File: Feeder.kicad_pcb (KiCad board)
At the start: 4 copper layers, 91 x 85 mm, 89 parts, among them J101 Conn_02x03_Odd_Even, J102 Conn_01x03_Pin, J103 Conn_01x02_Pin, U101 XBLW 24C02S(XBLW), U201 CMP6793RE, U301 CMP6793RE, U601 TPS562202, U701 TPS562202

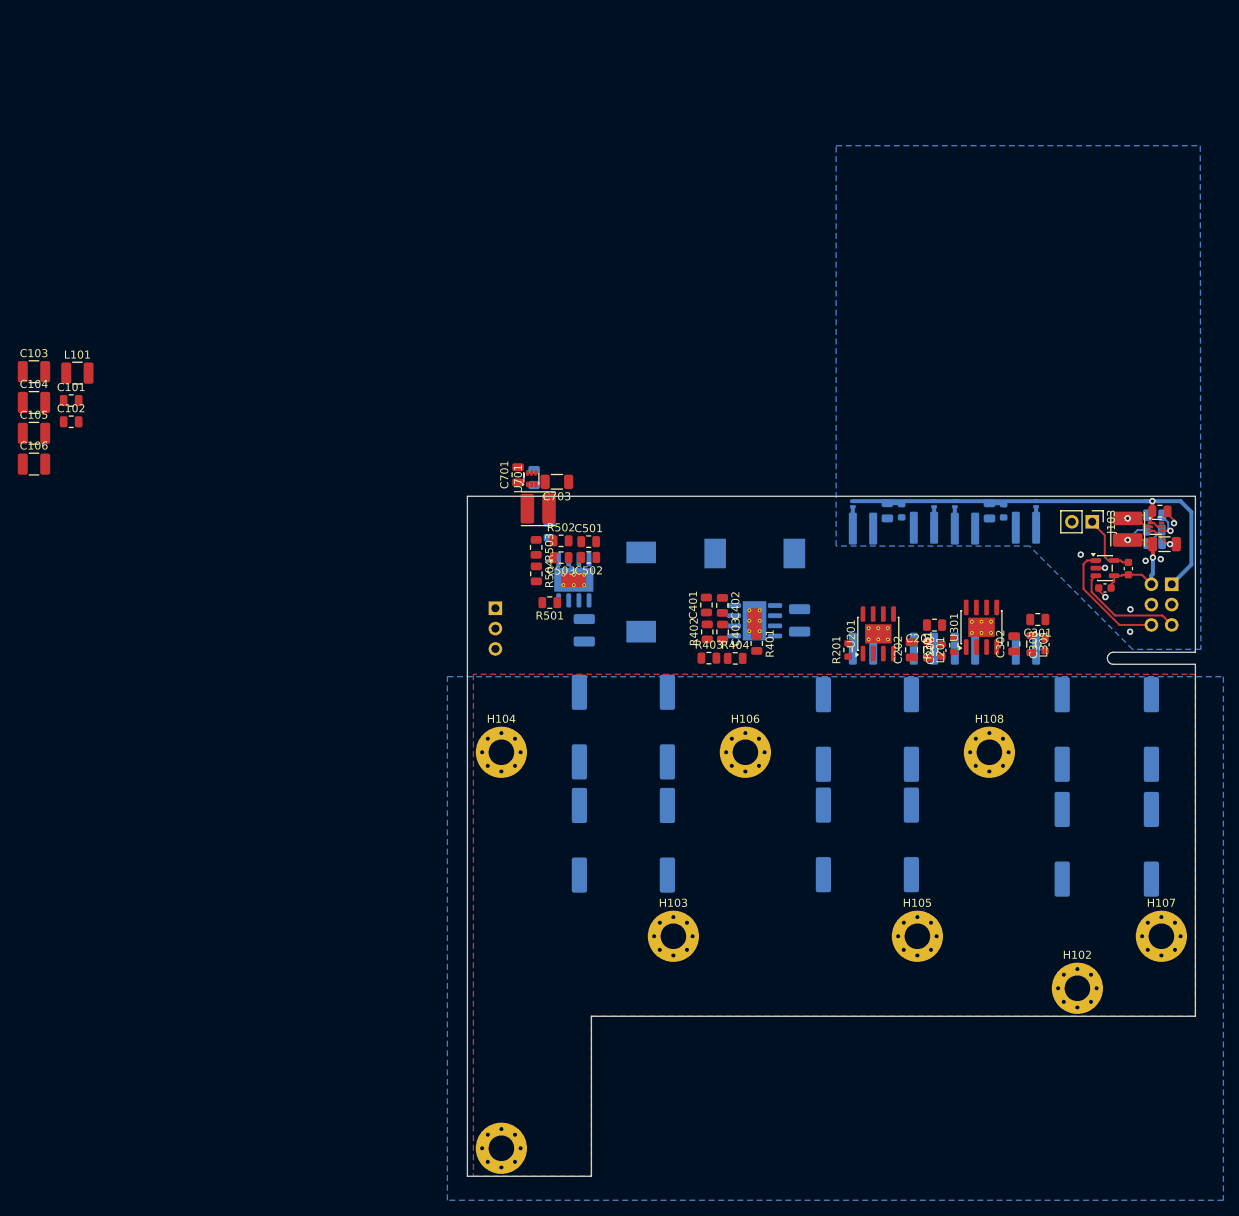
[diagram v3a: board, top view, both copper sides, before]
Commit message: feeder is routed
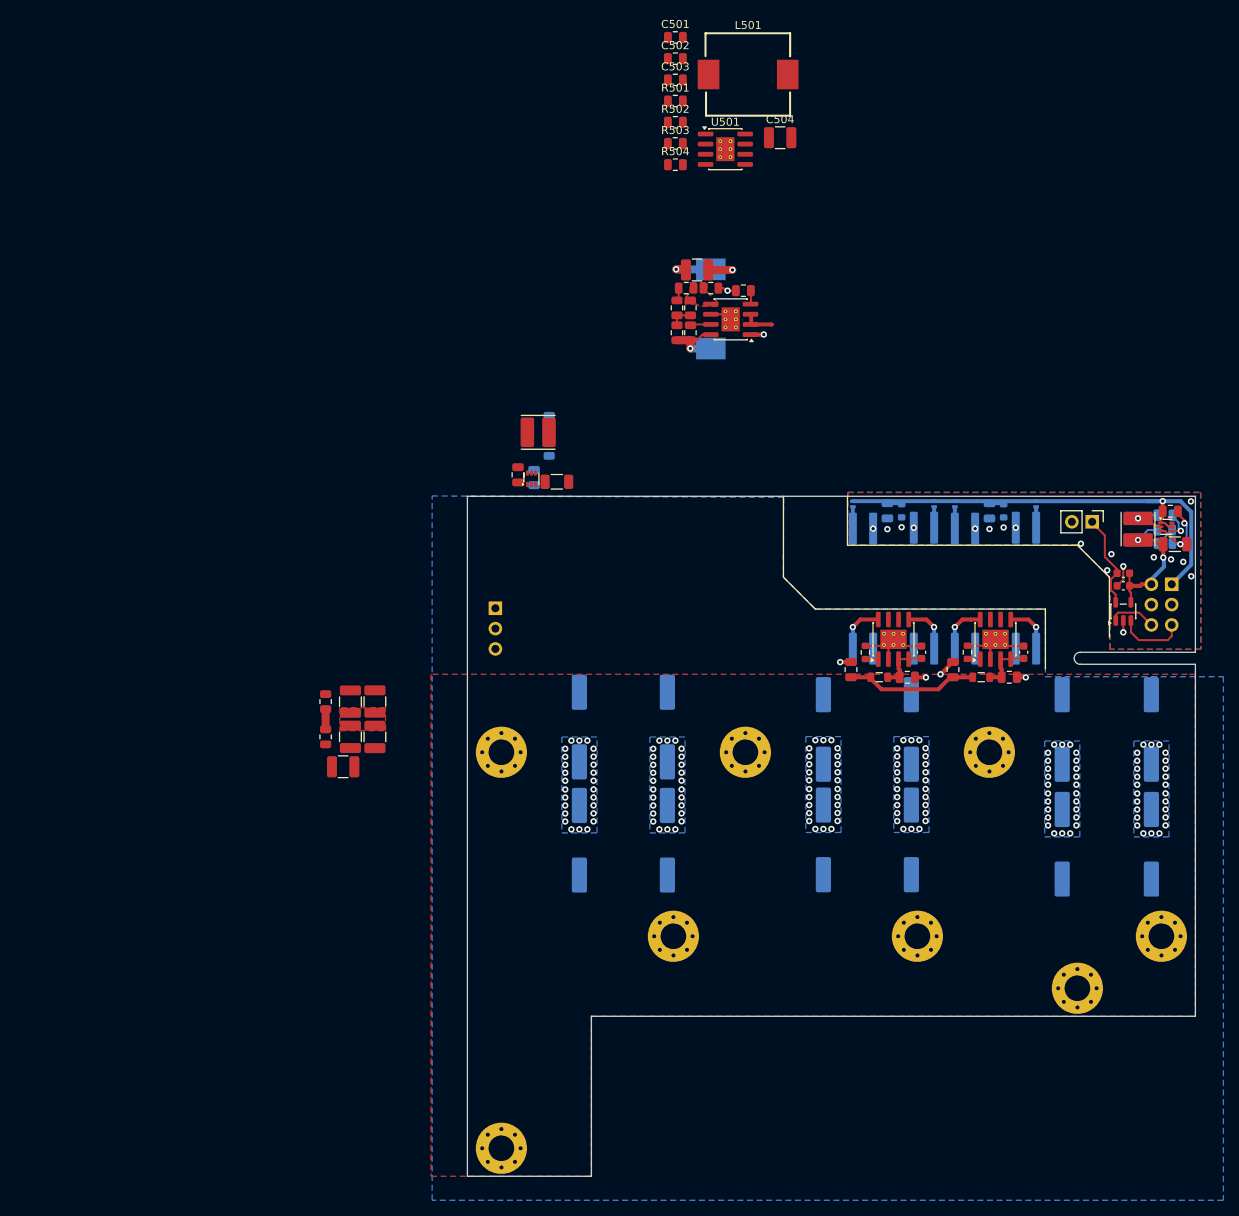
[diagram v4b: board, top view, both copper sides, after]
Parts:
- C404, C504, L501: moved to F.Cu
- U401, U501: footprint Package_SO:Texas_R-PDSO-G8_EP2.95x4.9mm_Mask2.4x3.1mm_ThermalVias -> Package_SO:SOIC-8-1EP_3.9x4.9mm_P1.27mm_EP2.29x3mm_ThermalVias; moved to F.Cu
- moved C504 66.3 mm to (43.6, -139.8), turned to 0 degrees
- moved L501 66.1 mm to (39.6, -147.7), turned to 0 degrees
- moved R501 64.6 mm to (30.5, -144.4), turned to 0 degrees
- moved C501 63.9 mm to (30.5, -152.3)
- moved C502 63.3 mm to (30.5, -149.7), turned to 0 degrees
- moved C503 61.4 mm to (30.5, -147.1), turned to 0 degrees
- moved C103 60.4 mm to (-10.1, -64.9), turned to 90 degrees
- moved L101 59.4 mm to (-11.0, -61.2), turned to 180 degrees
- moved U501 57.1 mm to (36.7, -138.4), turned to 0 degrees
- moved C105 57.1 mm to (-7.06, -64.9), turned to 90 degrees
- moved C104 54.4 mm to (-10.1, -69.3), turned to 90 degrees
- moved R502 54.2 mm to (30.5, -141.8)
- moved R504 54.0 mm to (30.5, -136.4), turned to 0 degrees
- moved R503 53.4 mm to (30.5, -139.1), turned to 0 degrees
- moved C101 52.7 mm to (-13.2, -64.9), turned to 90 degrees
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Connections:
- U401 pad 9: (no net) -> PGND
- U501 pad 9: (no net) -> PGND
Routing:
- net PGND: track 0.00 -> 30.6 mm, vias 0 -> 7
- net /buck/VOUT: track 0.00 -> 23.7 mm, vias 0 -> 1
- net Net-(U401-SW): track 0.00 -> 9.41 mm, vias 0 -> 1
- net Net-(J101-Pin_6): track 15.2 -> 5.90 mm
- net Net-(U201-EN): track 0.00 -> 6.74 mm
- net Net-(U301-EN): track 0.00 -> 6.74 mm
- net Net-(U201-VD2): track 0.00 -> 6.28 mm, vias 0 -> 1
- net Net-(U301-VD2): track 0.00 -> 6.27 mm, vias 0 -> 1
- net Net-(U301-VD1): track 0.00 -> 6.27 mm, vias 0 -> 1
- net Net-(U201-VD1): track 0.00 -> 6.26 mm, vias 0 -> 1
- net Net-(J101-Pin_5): track 14.0 -> 8.59 mm
- net DGND: track 9.14 -> 13.8 mm, vias 9 -> 20
- net /VIN_{FILT}: track 0.00 -> 3.86 mm
- net Net-(J103-Pin_1): track 8.27 -> 11.9 mm
- net Net-(C402-Pad2): track 0.00 -> 2.91 mm
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- added copper zone on B.Cu, net /VHigh
- added copper zone on F.Cu, net DGND
- added copper zone on F.Cu, net Net-(C103-Pad2)
- added copper zone on F.Cu, net Net-(U401-FB)
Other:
- outline, holes or cut-outs redrawn

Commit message: buck repeat layout done
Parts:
- L501: moved to B.Cu
- moved C501 42.1 mm to (23.6, -110.8), turned to -90 degrees
- moved L501 36.5 mm to (26.1, -113.7), turned to 90 degrees
- moved C502 36.5 mm to (23.6, -113.9), turned to -90 degrees
- moved C503 34.3 mm to (21.9, -113.9), turned to 90 degrees
- moved R502 32.1 mm to (21.9, -110.8), turned to 90 degrees
- moved C404 31.2 mm to (31.4, -92.1)
- moved C401 31.2 mm to (30.6, -84.3)
- moved C402 31.2 mm to (30.6, -87.4)
- moved C403 31.2 mm to (28.9, -87.4)
- moved L401 31.2 mm to (33.1, -87.2)
- moved R401 31.2 mm to (37.2, -89.5)
- moved R402 31.2 mm to (28.9, -84.3)
- moved R403 31.2 mm to (30.1, -89.8)
- moved R404 31.2 mm to (33.1, -89.8)
- moved U401 31.2 mm to (35.6, -85.9)
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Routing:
- net Net-(U501-SW): track 0.00 -> 9.41 mm, vias 0 -> 1
- net PGND: track 30.6 -> 39.5 mm, vias 7 -> 10
- net /buck1/VOUT: track 0.00 -> 7.16 mm, vias 0 -> 1
- net /VIN_{FILT}: track 3.86 -> 7.71 mm
- net Net-(C502-Pad2): track 0.00 -> 2.91 mm
- net Net-(U501-BST): track 0.00 -> 2.20 mm
- net Net-(U501-RT): track 0.00 -> 1.69 mm
- added copper zone on F.Cu, net Net-(U501-FB)

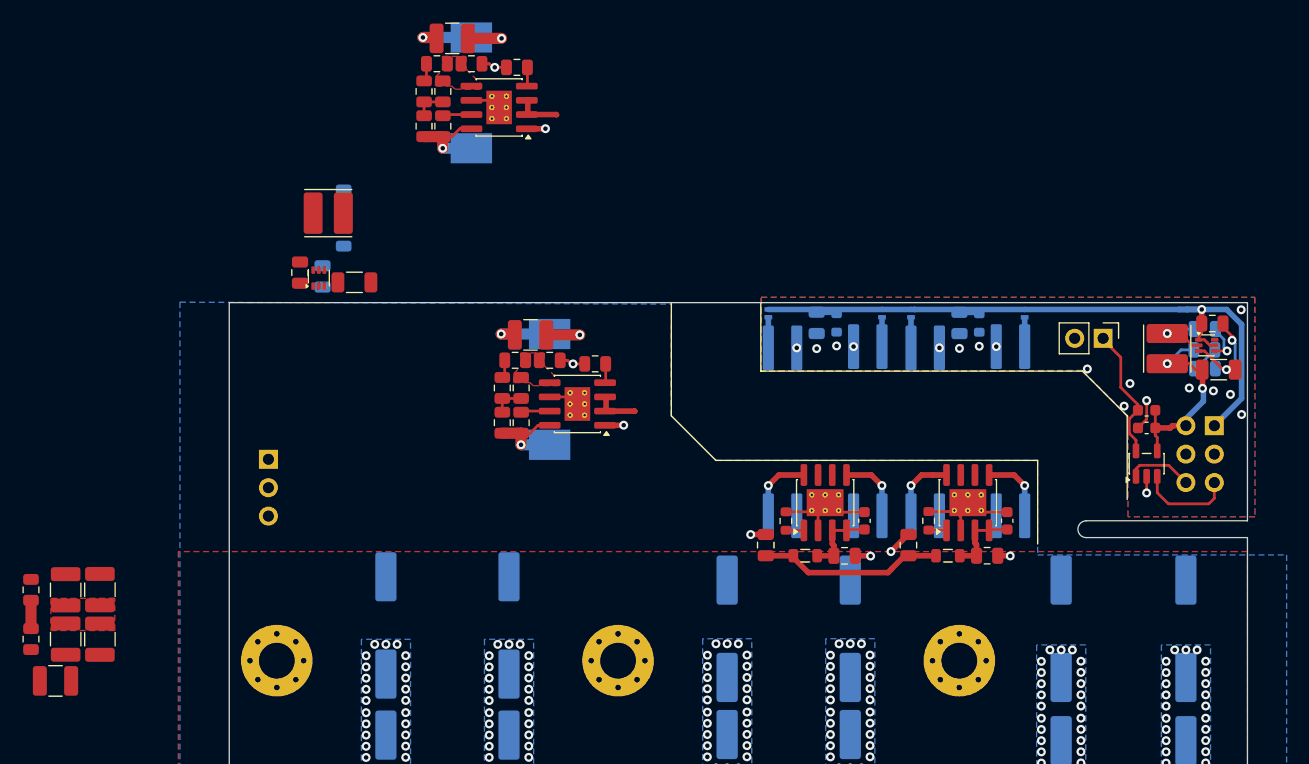
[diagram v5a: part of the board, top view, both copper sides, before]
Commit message: routing is done but violations are still present
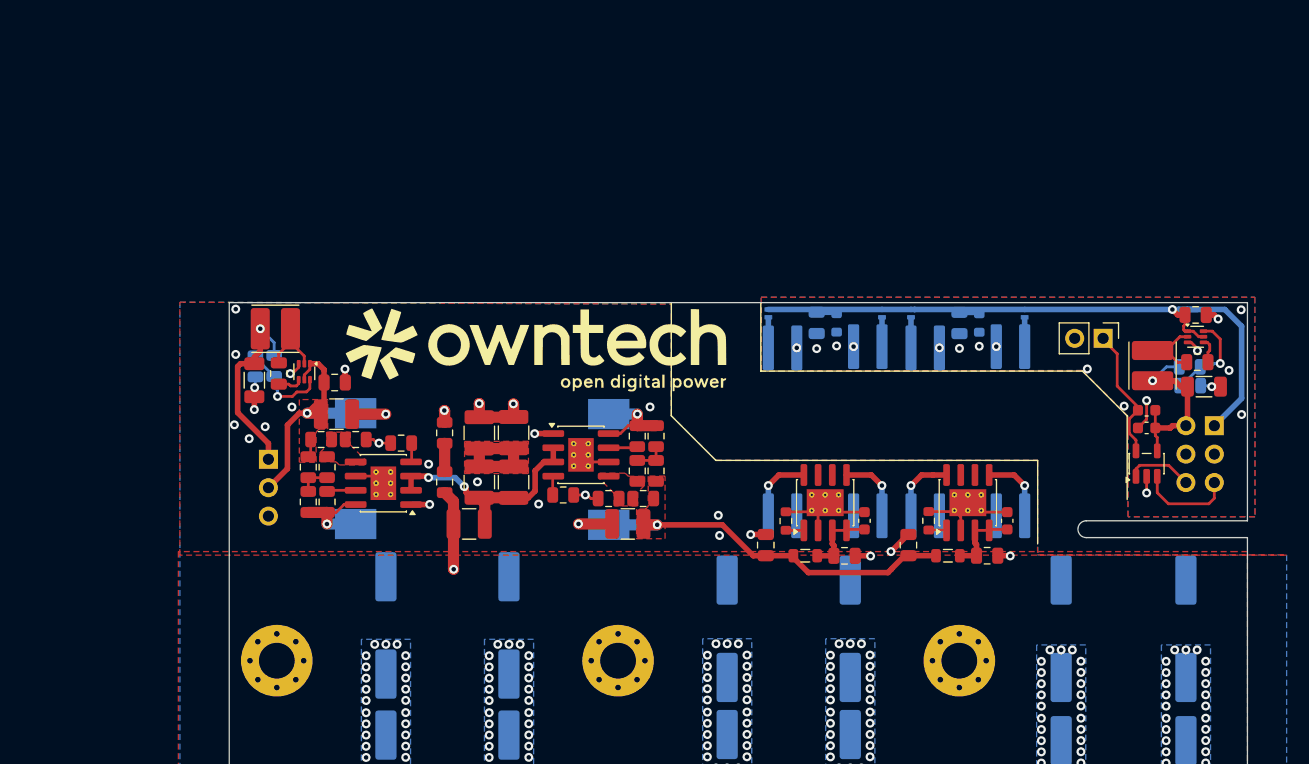
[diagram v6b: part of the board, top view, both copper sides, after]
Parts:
- added G***: LOGO, Footprints:owntech34mmneg, F.Cu at (31.9, -90.8)
- C602, C702: moved to F.Cu
- moved C101 39.5 mm to (23.8, -79.0)
- moved C102 39.5 mm to (23.8, -83.4)
- moved C103 39.5 mm to (26.9, -79.0)
- moved C104 39.5 mm to (26.9, -83.4)
- moved C105 39.5 mm to (29.9, -79.0)
- moved C106 39.5 mm to (29.9, -83.4)
- moved L101 39.5 mm to (25.9, -75.2), turned to 0 degrees
- moved C504 35.1 mm to (14.1, -85.0)
- moved R501 35.1 mm to (19.9, -82.4)
- moved C501 35.1 mm to (13.2, -77.2)
- moved C502 35.1 mm to (13.2, -80.3)
- moved C503 35.1 mm to (11.6, -80.3)
- moved L501 35.1 mm to (15.8, -80.2)
- moved R502 35.1 mm to (11.6, -77.2)
- moved R503 35.1 mm to (12.7, -82.8)
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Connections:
- J102 pad 1: /buck1/VOUT -> /dc-dc_12-6/VOUT
- J102 pad 2: /dc-dc_12-6/VOUT -> /buck1/VOUT
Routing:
- net /dc-dc_12-6/VOUT: track 0.00 -> 17.3 mm, vias 0 -> 1
- net /buck1/VOUT: track 7.16 -> 23.2 mm
- net /VIN_{FILT}: track 7.71 -> 21.2 mm, vias 0 -> 2
- net PGND: track 39.5 -> 51.8 mm, vias 10 -> 29
- net /buck/VOUT: track 23.7 -> 33.1 mm
- net Net-(C103-Pad2): track 0.00 -> 9.36 mm
- net Net-(U701-VFB): track 0.00 -> 8.42 mm, vias 0 -> 1
- net /VHigh: track 0.00 -> 7.19 mm, vias 156 -> 157
- net Net-(U701-SW): track 0.00 -> 6.90 mm
- net Net-(U601-VFB): track 2.53 -> 8.42 mm, vias 0 -> 1
- net DGND: track 13.8 -> 9.30 mm, vias 20 -> 18
- net Net-(U701-VBST): track 0.00 -> 2.27 mm
- net +5V_DGND: track 18.4 -> 16.4 mm, vias 2 -> 1
- net Net-(U601-VBST): track 3.49 -> 2.27 mm, vias 1 -> 0
- net Net-(U601-SW): track 5.84 -> 6.90 mm, vias 1 -> 0
- added copper zone on F.Cu, net /buck/VOUT
- added copper zone on F.Cu, net /buck1/VOUT
- added copper zone on F.Cu, net PGND

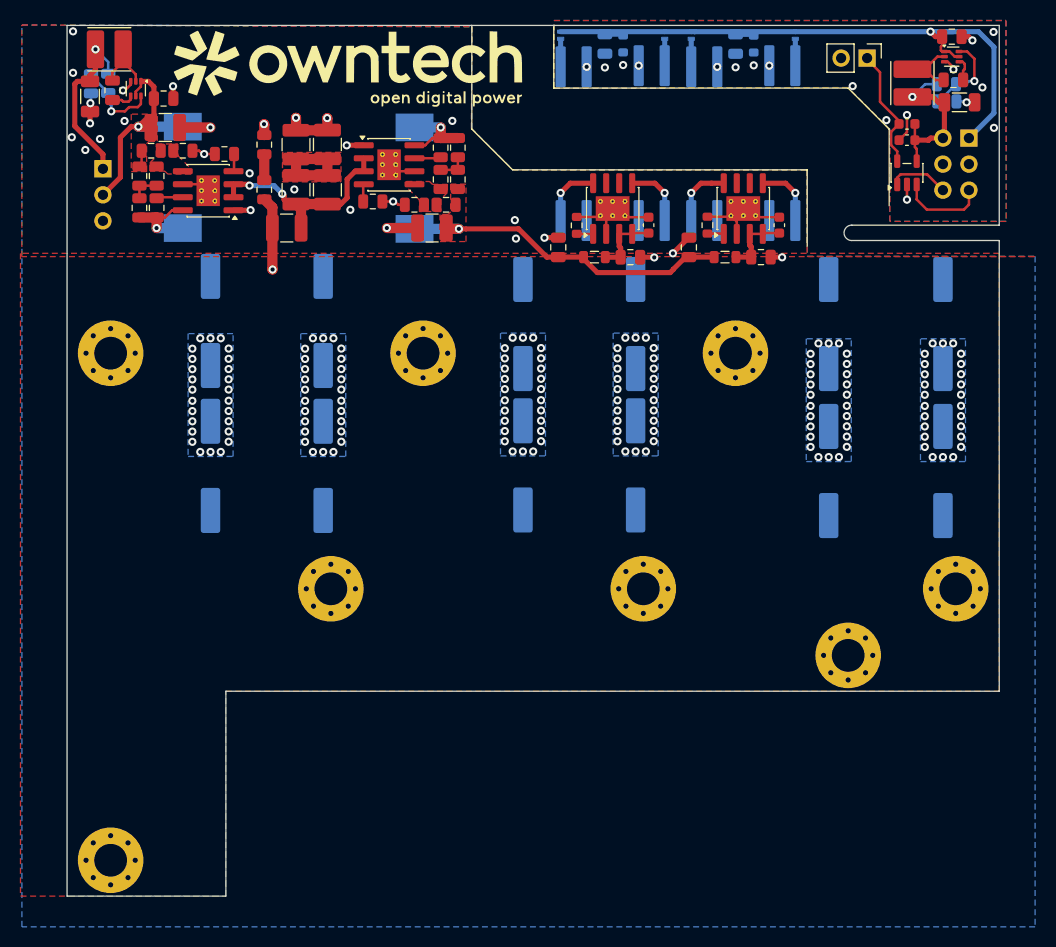
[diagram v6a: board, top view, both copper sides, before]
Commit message: no erc errors
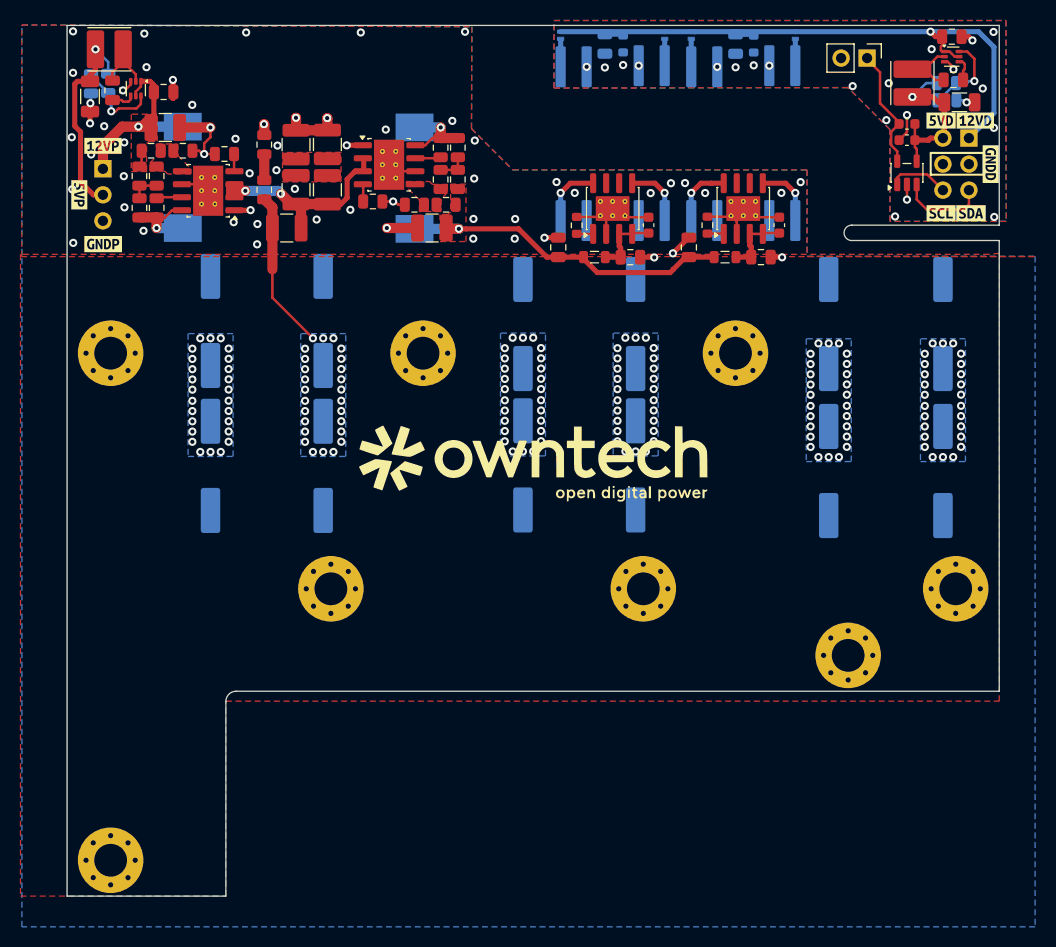
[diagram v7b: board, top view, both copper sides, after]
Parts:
- added kibuzzard-6A746332: G***, kibuzzard-6A746332, F.Cu at (5.69, -78.5)
- added kibuzzard-6A746332: G***, kibuzzard-6A746332, B.Cu at (5.69, -78.5)
- added kibuzzard-6A746339: G***, kibuzzard-6A746339, F.Cu at (8.02, -73.7)
- added kibuzzard-6A746339: G***, kibuzzard-6A746339, B.Cu at (8.02, -73.7)
- added kibuzzard-6A746342: G***, kibuzzard-6A746342, F.Cu at (8.00, -83.2)
- added kibuzzard-6A746342: G***, kibuzzard-6A746342, B.Cu at (8.00, -83.2)
- added kibuzzard-6A74635F: G***, kibuzzard-6A74635F, F.Cu at (89.8, -85.7)
- added kibuzzard-6A74635F: G***, kibuzzard-6A74635F, B.Cu at (89.8, -86.3)
- added kibuzzard-6A746363: G***, kibuzzard-6A746363, F.Cu at (93.2, -85.7)
- added kibuzzard-6A746363: G***, kibuzzard-6A746363, B.Cu at (93.2, -86.3)
- added kibuzzard-6A746399: G***, kibuzzard-6A746399, F.Cu at (92.7, -76.7)
- added kibuzzard-6A746399: G***, kibuzzard-6A746399, B.Cu at (92.7, -76.7)
- added kibuzzard-6A74639F: G***, kibuzzard-6A74639F, F.Cu at (89.8, -76.7)
- added kibuzzard-6A74639F: G***, kibuzzard-6A74639F, B.Cu at (89.8, -76.7)
- added kibuzzard-6A7463BC: G***, kibuzzard-6A7463BC, F.Cu at (94.7, -81.5)
- added kibuzzard-6A7463BC: G***, kibuzzard-6A7463BC, B.Cu at (87.7, -81.3)
- added kibuzzard-6A7463BC: G***, kibuzzard-6A7463BC, B.Cu at (94.8, -81.5)
- U401, U501: footprint Package_SO:SOIC-8-1EP_3.9x4.9mm_P1.27mm_EP2.29x3mm_ThermalVias -> Package_SO:Texas_R-PDSO-G8_EP2.95x4.9mm_Mask2.4x3.1mm_ThermalVias
- moved G*** 42.6 mm to (50.0, -52.2)
- moved C701 0.64 mm to (13.9, -88.5)
- moved R601 0.11 mm to (90.3, -89.4)
- moved R602 0.11 mm to (90.4, -87.7)
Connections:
- net /buck/VOUT renamed /12V_P_0
- net Net-(J101-Pin_5) renamed /SDA
- net Net-(J101-Pin_6) renamed /SCL
- net Net-(J103-Pin_1) renamed /WP
- C503 pad 2: /buck1/VOUT -> +12V_PGND
- C504 pad 1: /buck1/VOUT -> +12V_PGND
- C701 pad 1: /buck1/VOUT -> +12V_PGND
- C703 pad 1: /dc-dc_12-6/VOUT -> +5V_PGND
- J102 pad 1: /dc-dc_12-6/VOUT -> +12V_PGND
- J102 pad 2: /buck1/VOUT -> +5V_PGND
- L501 pad 2: /buck1/VOUT -> +12V_PGND
- L701 pad 2: /dc-dc_12-6/VOUT -> +5V_PGND
- R503 pad 1: /buck1/VOUT -> +12V_PGND
- R701 pad 1: /dc-dc_12-6/VOUT -> +5V_PGND
- U701 pad 1: /buck1/VOUT -> +12V_PGND
- U701 pad 5: /buck1/VOUT -> +12V_PGND
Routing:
- net /buck1/VOUT: track 23.2 -> 0.00 mm, vias 1 -> 0
- net +12V_PGND: track 0.00 -> 21.0 mm, vias 0 -> 1
- net +5V_PGND: track 0.00 -> 20.4 mm, vias 0 -> 1
- net /dc-dc_12-6/VOUT: track 17.3 -> 0.00 mm, vias 1 -> 0
- net Net-(C103-Pad2): track 9.36 -> 0.04 mm
- net /VHigh: track 7.19 -> 15.5 mm, vias 157 -> 156
- net /VIN_{FILT}: track 21.2 -> 26.4 mm
- net PGND: track 51.8 -> 55.3 mm, vias 29 -> 60
- net +12V_DGND: track 62.9 -> 62.0 mm
- net DGND: track 9.30 -> 9.39 mm, vias 18 -> 22
- added copper zone on F.Cu, net +12V_PGND
- removed copper zone on F.Cu, net /buck1/VOUT
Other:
- outline, holes or cut-outs redrawn
